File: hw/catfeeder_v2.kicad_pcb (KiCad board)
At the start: 2 copper layers, 73 x 69.2 mm, 20 parts, among them J1 CONN_BEEPER, J11 CONN_MOT2, J2 CONN_SENSOR_ADC, J3 CONN_SENSOR, J4 CONN_MOT1, J6 CONN_LCD, J8 CONN_POWER, Q1 IRLML6402, U1 NodeMCU_1.0_(ESP-12E), U2 LM317_3PinPackage

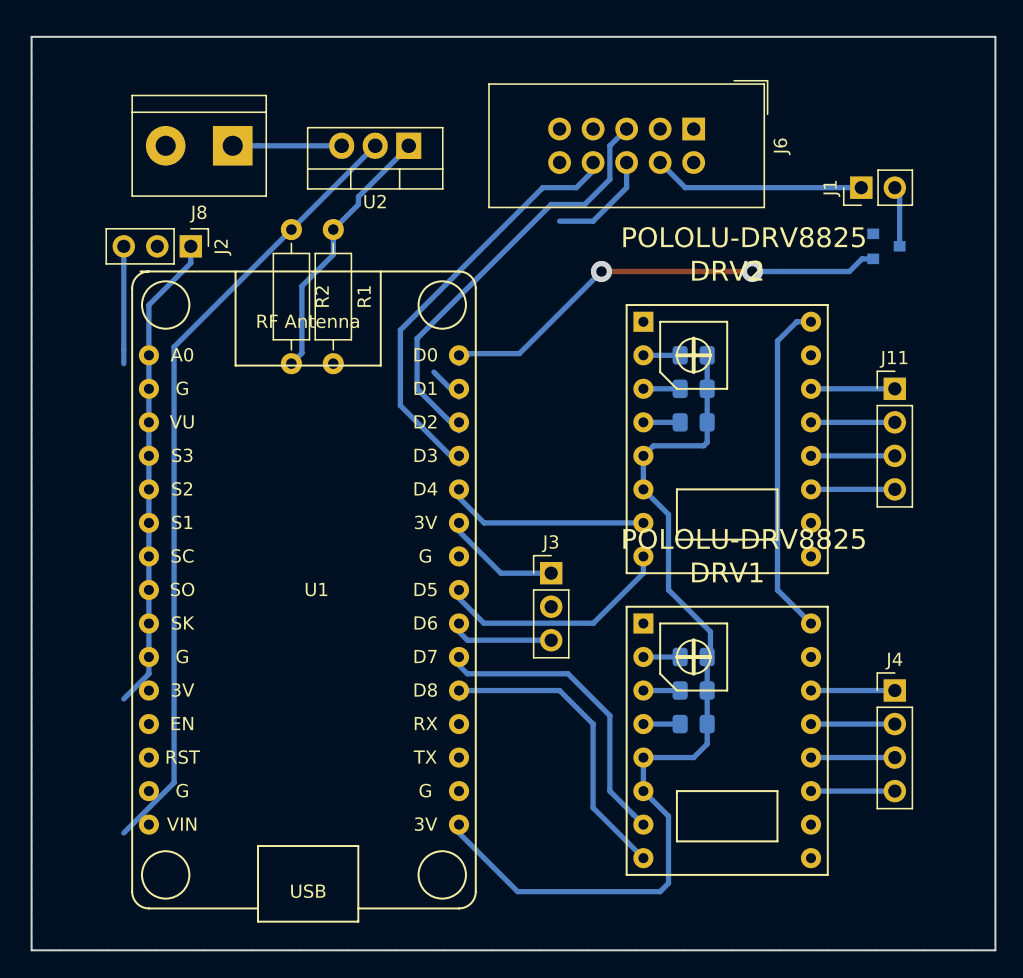
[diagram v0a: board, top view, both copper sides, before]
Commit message: Add mounting holes
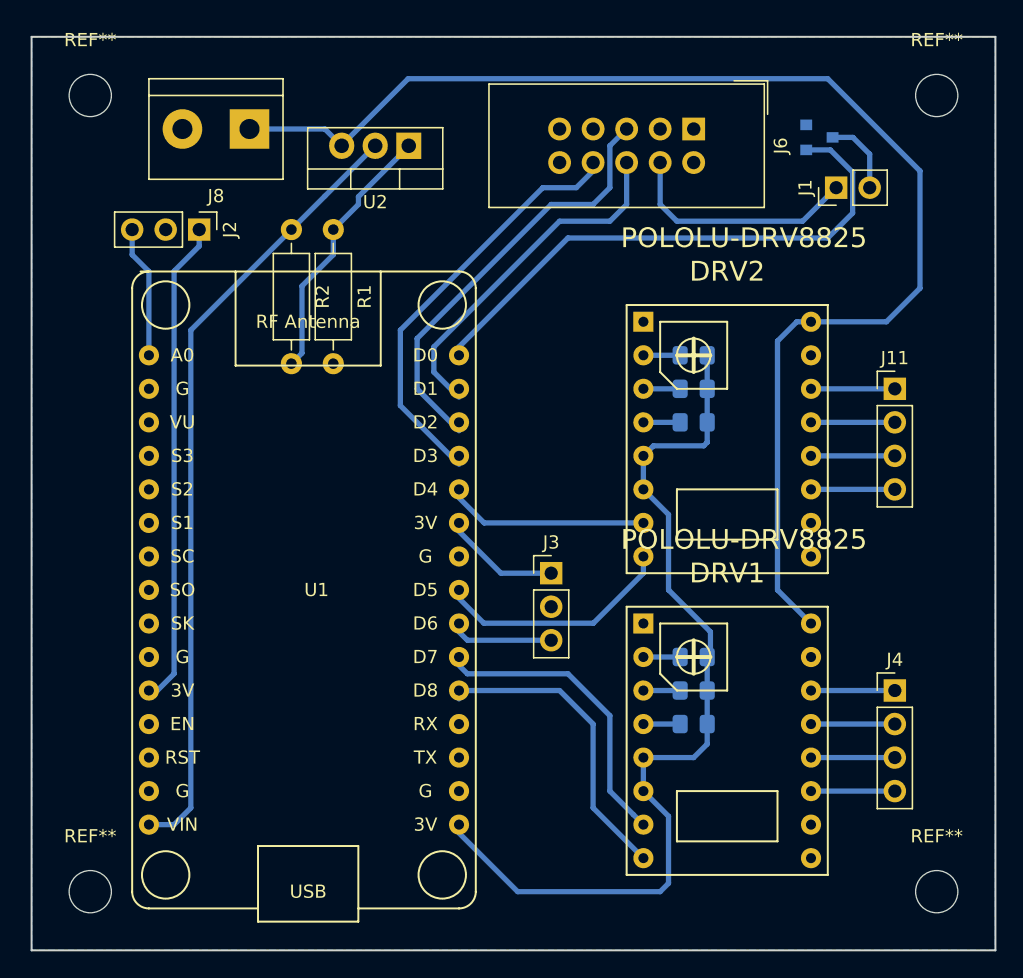
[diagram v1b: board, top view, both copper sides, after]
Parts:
- added REF**: MountingHole_3.2mm_M3, MountingHole:MountingHole_3.2mm_M3, F.Cu at (187.3, 57.1)
- added REF**: MountingHole_3.2mm_M3, MountingHole:MountingHole_3.2mm_M3, F.Cu at (187.3, 117.5)
- added REF**: MountingHole_3.2mm_M3, MountingHole:MountingHole_3.2mm_M3, F.Cu at (123.2, 117.5)
- added REF**: MountingHole_3.2mm_M3, MountingHole:MountingHole_3.2mm_M3, F.Cu at (123.2, 57.1)
- moved Q1 9.69 mm to (178.4, 60.3)
- moved J1 1.91 mm to (179.7, 64.1)
- moved J8 1.80 mm to (135.3, 59.7)
- moved J2 1.42 mm to (131.4, 67.3)
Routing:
- net +12V: track 33.9 -> 100.1 mm
- net /I2C_SCL: track 10.7 -> 26.9 mm
- net /BEEPER: track 34.7 -> 42.0 mm, vias 2 -> 0
- net +3V3: track 130.3 -> 132.9 mm
- net Net-(J1-Pad2): track 4.60 -> 5.88 mm
- net /SENSOR_ANALOG_IN: track 8.89 -> 10.1 mm

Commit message: hw: Add missing pullup resistors for I2C
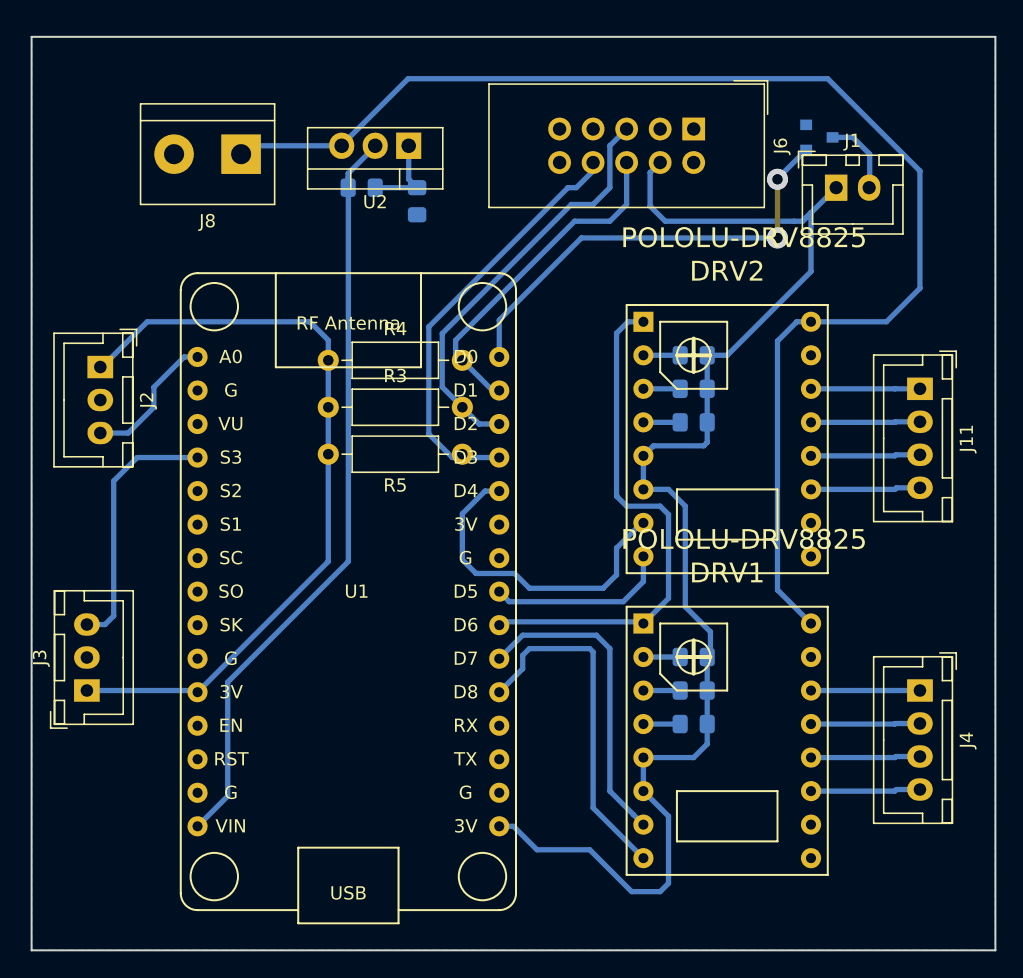
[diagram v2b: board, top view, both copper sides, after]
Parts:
- removed REF** (x4): MountingHole_3.2mm_M3, MountingHole:MountingHole_3.2mm_M3
- added R3: R, Resistor_THT:R_Axial_DIN0207_L6.3mm_D2.5mm_P10.16mm_Horizontal, F.Cu at (141.2, 80.8)
- added R4: R, Resistor_THT:R_Axial_DIN0207_L6.3mm_D2.5mm_P10.16mm_Horizontal, F.Cu at (141.2, 77.2)
- added R5: R, Resistor_THT:R_Axial_DIN0207_L6.3mm_D2.5mm_P10.16mm_Horizontal, F.Cu at (151.4, 84.3)
- J1: footprint Connector_PinHeader_2.54mm:PinHeader_1x02_P2.54mm_Vertical -> Connector_JST:JST_XH_B02B-XH-A_1x02_P2.50mm_Vertical
- J11, J4: footprint Connector_PinHeader_2.54mm:PinHeader_1x04_P2.54mm_Vertical -> Connector_JST:JST_XH_B04B-XH-A_1x04_P2.50mm_Vertical
- J2, J3: footprint Connector_PinHeader_2.54mm:PinHeader_1x03_P2.54mm_Vertical -> Connector_JST:JST_XH_B03B-XH-A_1x03_P2.50mm_Vertical
- R1, R2: footprint Resistor_THT:R_Axial_DIN0207_L6.3mm_D2.5mm_P10.16mm_Horizontal -> Resistor_SMD:R_0805_2012Metric_Pad1.15x1.40mm_HandSolder; moved to B.Cu
- moved J3 36.3 mm to (122.9, 102.2), turned to 90 degrees
- moved J2 12.8 mm to (124.0, 77.7)
- moved R1 6.70 mm to (148.0, 65.2)
- moved R2 6.20 mm to (143.8, 64.1), turned to 0 degrees
- moved U1 3.05 mm to (142.7, 96.0)
- moved J8 2.01 mm to (134.6, 61.6)
- moved J11 1.91 mm to (186.1, 79.4), turned to 270 degrees
- moved J4 1.91 mm to (186.1, 102.2), turned to 270 degrees
- turned J1 to 0 degrees
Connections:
- DRV1 pad 1: (no net) -> /MOT_ENABLE
- DRV2 pad 1: (no net) -> /MOT_ENABLE
- J3 pad 3: /SENSOR_IN -> /SENSOR_1
- U1 pad 22: /SENSOR_IN -> /MOT_ENABLE
- U1 pad 4: (no net) -> /SENSOR_1
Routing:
- net /MOT_ENABLE: track 0.00 -> 39.4 mm
- net +3V3: track 132.9 -> 161.4 mm
- net /SENSOR_1: track 0.00 -> 19.6 mm
- net Net-(R1-Pad1): track 20.2 -> 6.61 mm
- net /MOT2_STEP: track 14.8 -> 24.8 mm
- net /BEEPER: track 42.0 -> 34.0 mm, vias 0 -> 2
- net /SENSOR_IN: track 7.25 -> 0.00 mm
- net /MOT2_DIR: track 17.6 -> 13.8 mm
- net /MOT1_DIR: track 23.2 -> 26.4 mm
- net VCC: track 59.7 -> 57.2 mm
- net /SENSOR_ANALOG_IN: track 10.1 -> 12.0 mm
- net Net-(DRV2-Pad11): track 6.35 -> 8.30 mm
- net Net-(DRV1-Pad11): track 6.35 -> 8.30 mm
- net Net-(DRV2-Pad12): track 6.35 -> 8.29 mm
- net Net-(DRV1-Pad12): track 6.35 -> 8.29 mm
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
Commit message: Move INTPIN to GPIO3
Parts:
- removed R5: R, Resistor_THT:R_Axial_DIN0207_L6.3mm_D2.5mm_P10.16mm_Horizontal
- moved J3 18.0 mm to (125.0, 84.3), turned to 270 degrees
- moved J2 5.18 mm to (125.0, 72.6)
- moved J8 2.54 mm to (132.1, 61.5)
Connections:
- U1 pad 19: (no net) -> /LCD_INT
- U1 pad 27: /LCD_INT -> (no net)
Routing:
- net /LCD_INT: track 32.2 -> 50.4 mm
- net /SENSOR_1: track 19.6 -> 9.37 mm
- net /SENSOR_ANALOG_IN: track 12.0 -> 6.63 mm
- net +3V3: track 161.4 -> 165.8 mm
- net +12V: track 100.5 -> 103.0 mm
